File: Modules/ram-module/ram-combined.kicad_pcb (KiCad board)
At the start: 4 copper layers, 192 x 81.5 mm, 63 parts, among them J1 Conn_01x08, J2 Conn_01x08, J3 Conn_01x10, J4 Conn_01x02, J5 Screw_Terminal_01x02, J6 Conn_01x16, J7 Conn_01x08, J8 Conn_01x08, SW1 SW_SPDT, SW2 SW_Push, SW3 SW_DIP_x08, SW4 SW_DIP_x08, SW5 SW_DIP_x08, U1 74LS00, U10 74LS173, U11 74LS245, U12 74LS173, U13 74LS245, U14 74LS173, U15 74LS157, U16 74LS173, U17 74LS157, U2 74LS32, U3 74LS157, U4 74LS157, U5 74LS173, U6 74LS157, U7 74LS157, U8 74LS173, U9 IS61C1024-15N

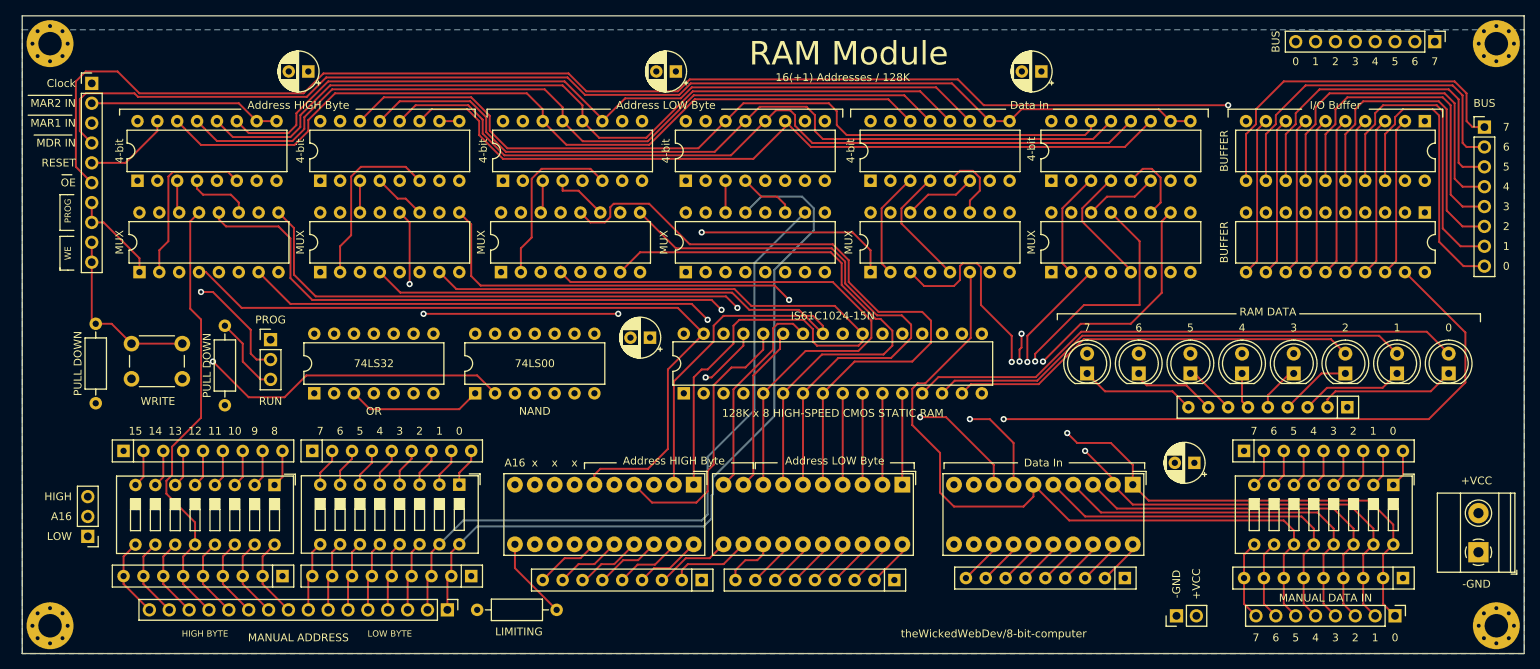
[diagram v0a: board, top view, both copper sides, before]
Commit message: [RAM Module] Updates after receiving PCB
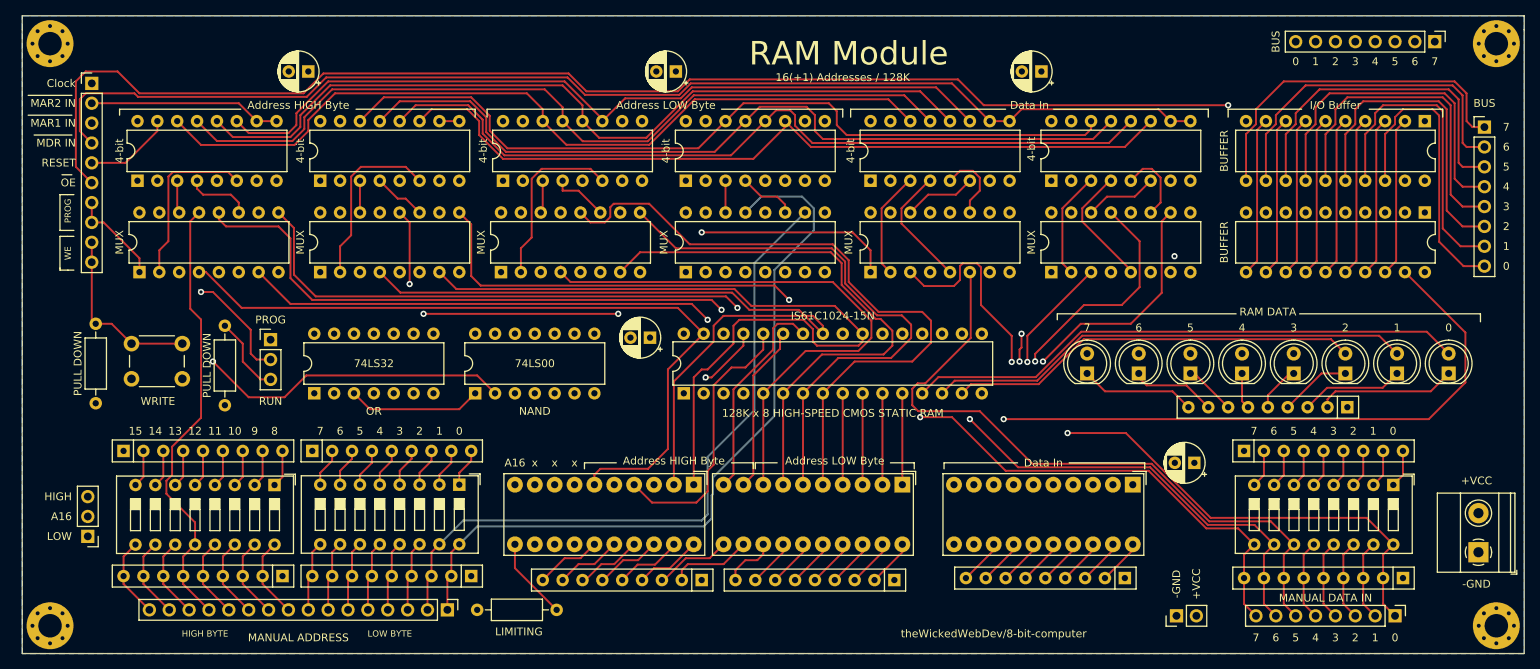
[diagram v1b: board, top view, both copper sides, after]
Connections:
- BAR3 pad 1: /MANUAL_DATA_00 -> D0
- BAR3 pad 2: /MANUAL_DATA_01 -> D1
- BAR3 pad 3: /MANUAL_DATA_02 -> D2
- BAR3 pad 4: /MANUAL_DATA_03 -> D3
- BAR3 pad 5: /MANUAL_DATA_04 -> D4
- BAR3 pad 6: /MANUAL_DATA_05 -> D5
- BAR3 pad 7: /MANUAL_DATA_06 -> D6
- BAR3 pad 8: /MANUAL_DATA_07 -> D7
- RN10 pad 1: Net-(RN10-Pad1) -> GND
- U17 pad 13: /MANUAL_DATA_01 -> /MANUAL_DATA_03
- U17 pad 6: /MANUAL_DATA_03 -> /MANUAL_DATA_01
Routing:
- net D4: track 55.6 -> 124.1 mm
- net D5: track 44.7 -> 102.5 mm
- net D7: track 44.3 -> 90.5 mm
- net D6: track 38.7 -> 82.7 mm
- net D0: track 40.7 -> 81.6 mm, vias 0 -> 1
- net D3: track 31.6 -> 71.7 mm
- net D2: track 23.7 -> 63.6 mm
- net D1: track 40.4 -> 71.4 mm
- net /MANUAL_DATA_05: track 95.9 -> 87.2 mm
- net /MANUAL_DATA_02: track 95.9 -> 89.2 mm
- net /MANUAL_DATA_03: track 91.3 -> 87.4 mm, vias 2 -> 1
- net /MANUAL_DATA_04: track 91.8 -> 88.2 mm
- net /MANUAL_DATA_06: track 107.3 -> 104.2 mm
- net /MANUAL_DATA_00: track 86.9 -> 83.9 mm
- net /MANUAL_DATA_01: track 98.1 -> 96.2 mm
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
